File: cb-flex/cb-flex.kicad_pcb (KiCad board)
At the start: 4 copper layers, 81 x 76 mm, 84 parts, among them P1 CONN_01X14, P2 CONN_01X14, P3 CONN_01X01, P4 CONN_01X04, P5 CONN_01X02, P6 CONN_01X09, Q1 Q_NMOS_GSD, Q2 Q_NMOS_GSD, SW1 SW_PUSH_SMALL, U1 BMP180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

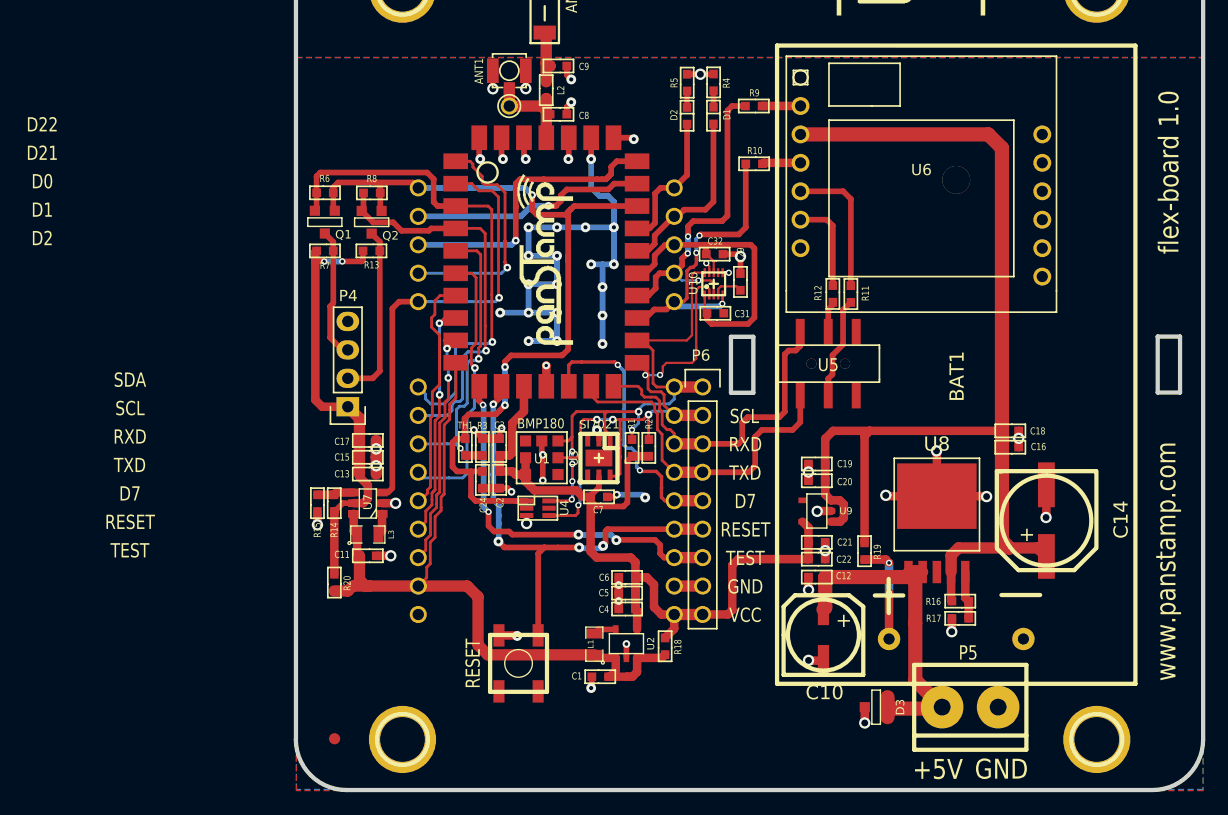
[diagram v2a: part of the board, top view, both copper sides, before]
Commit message: PCB layour finished
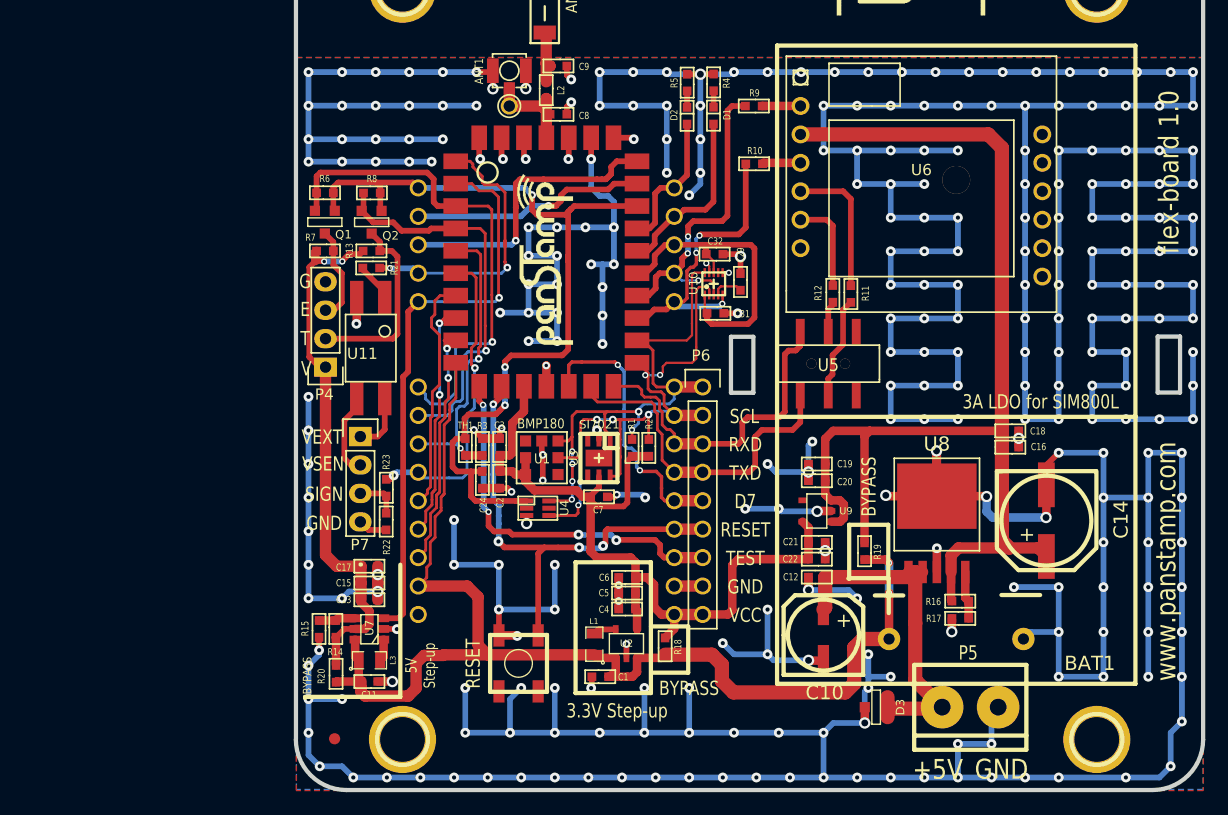
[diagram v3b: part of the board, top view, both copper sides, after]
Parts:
- added P7: CONN_01X04, Pin_Headers:Pin_Header_Straight_1x04, F.Cu at (198.6, 70.5)
- added R21: 1k, mysmd:SM0603S, F.Cu at (199.6, 55.5)
- added R22: 150, mysmd:SM0603S, F.Cu at (200.9, 78.1)
- added R23: 1k, mysmd:SM0603S, F.Cu at (200.9, 75.1)
- added U11: SSR, mysmd:SMT-DIP-4, F.Cu at (199.6, 62.6)
- moved C11 11.2 mm to (199.4, 92.4)
- moved L3 11.2 mm to (199.4, 90.5)
- moved R14 11.2 mm to (196.4, 87.7)
- moved R15 11.2 mm to (194.9, 87.7)
- moved U7 11.2 mm to (199.4, 87.7)
- moved C13 11.2 mm to (199.4, 85.1)
- moved C15 11.2 mm to (199.4, 83.6)
- moved C17 11.2 mm to (199.4, 82.1)
- moved R20 8.15 mm to (196.5, 91.7)
- moved P4 4.06 mm to (195.5, 64.3)
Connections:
- net /D12 renamed 4-20mA_INP
- net /D17 renamed EN_4-20mA_SENS
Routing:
- net GND: track 136.2 -> 927.9 mm, vias 64 -> 303
- net +BATT: track 94.0 -> 126.7 mm
- net EN_EXTERNAL: track 40.4 -> 51.1 mm
- net VDD: track 39.7 -> 49.2 mm
- net Net-(P7-Pad2): track 0.00 -> 7.48 mm
- net Net-(P7-Pad1): track 0.00 -> 5.21 mm
- net Net-(P7-Pad3): track 0.00 -> 3.94 mm
- net EN_4-20mA_SENS: track 21.6 -> 25.2 mm, vias 1 -> 2
- net Net-(R21-Pad1): track 0.00 -> 3.47 mm
- net Net-(P4-Pad3): track 11.8 -> 8.54 mm
- net 4-20mA_INP: track 25.6 -> 28.7 mm, vias 1 -> 2
- net Net-(P4-Pad2): track 15.7 -> 17.2 mm
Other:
- board text added: "3.3V Step-up"
- board text added: "3A LDO for SIM800L"
- board text added: "5V Step-up"
- board text added: "BYPASS"
- board text added: "E"
- board text added: "G"
- board text added: "SIGN"
- board text added: "T"
- board text added: "V"
- board text added: "VEXT"
- board text added: "VSEN"
- board text removed: "D0"
- board text removed: "D1"
- board text removed: "D2"
- board text removed: "D21"
- board text removed: "D22"
- board text removed: "SDA"

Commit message: PCB layout finished
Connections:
- P1 pad 10: /D11 -> 4-20mA_INP
- P1 pad 9: 4-20mA_INP -> VEXT
- P7 pad 1: Net-(P7-Pad1) -> VEXT
- PS1 pad 6: 4-20mA_INP -> VEXT
- PS1 pad 7: /D11 -> 4-20mA_INP
- U11 pad 4: Net-(P7-Pad1) -> VEXT
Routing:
- net VEXT: track 0.00 -> 38.4 mm, vias 0 -> 1
- net /D11: track 21.2 -> 0.00 mm
- net Net-(P7-Pad1): track 5.21 -> 0.00 mm
- net 4-20mA_INP: track 28.7 -> 25.6 mm, vias 2 -> 1
